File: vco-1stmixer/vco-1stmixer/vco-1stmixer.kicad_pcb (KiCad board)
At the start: 2 copper layers, 91.7 x 48.8 mm, 48 parts, among them J101 VCO Control In, J102 1st IF Out, J103 VCO Sample, J104 RF In, J105 Conn_01x02, U101 POS-200, U102 MAV-11, U103 MAV-11, U104 TUF-1H+

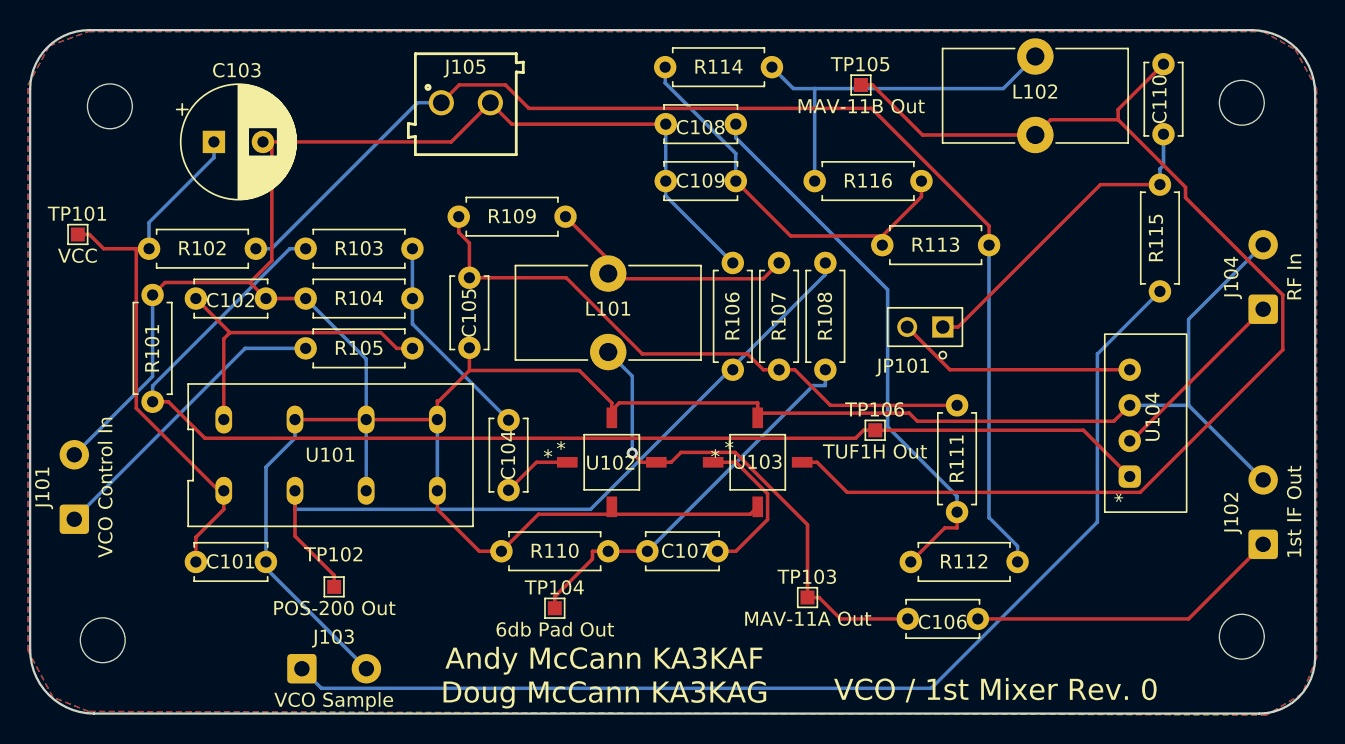
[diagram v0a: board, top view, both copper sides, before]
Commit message: minor changes to 5 boards
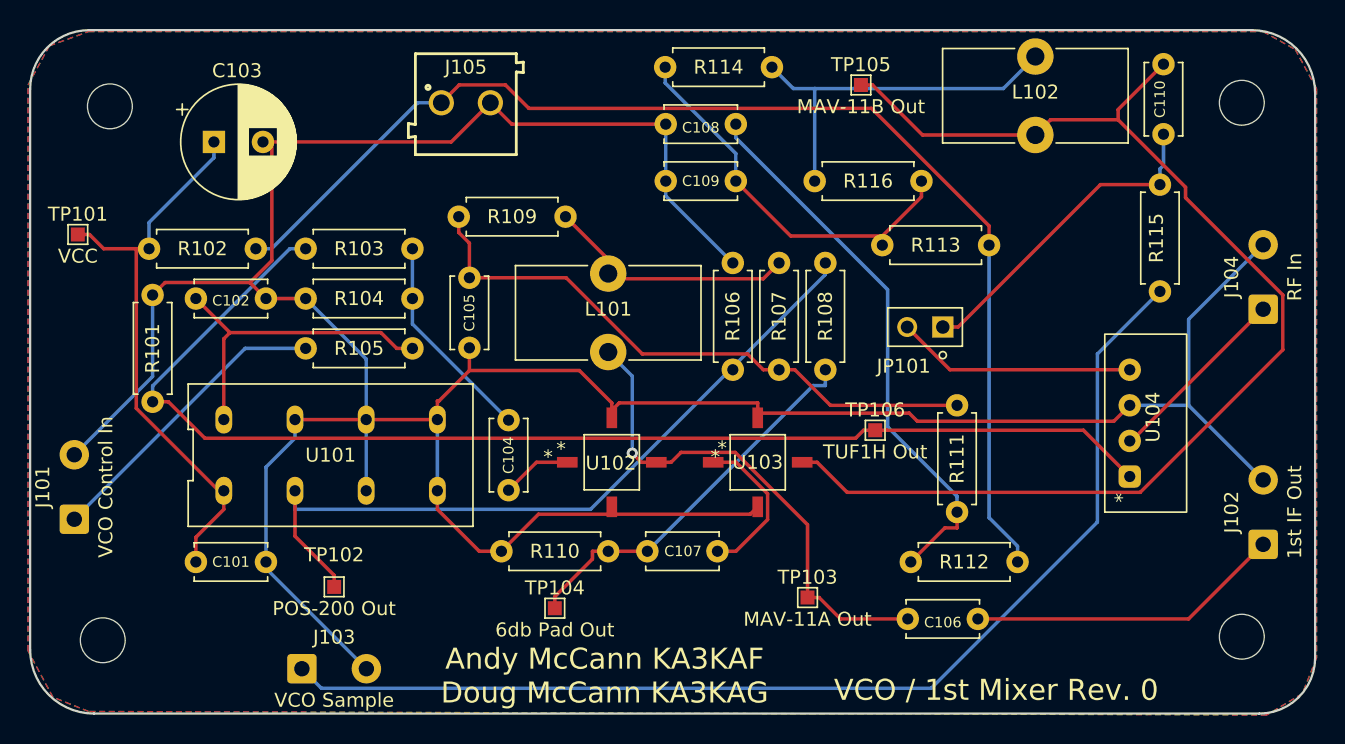
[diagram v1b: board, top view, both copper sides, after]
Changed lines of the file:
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@@
   )
   (setup
+    (stackup
+      (layer "F.SilkS" (type "Top Silk Screen"))
+      (layer "F.Paste" (type "Top Solder Paste"))
+      (layer "F.Mask" (type "Top Solder Mask") (thickness 0.01))
+      (layer "F.Cu" (type "copper") (thickness 0.035))
+      (layer "dielectric 1" (type "core") (thickness 1.51) (material "FR4") (epsilon_r 4.5) (loss_tangent 0.02))
+      (layer "B.Cu" (type "copper") (thickness 0.035))
+      (layer "B.Mask" (type "Bottom Solder Mask") (thickness 0.01))
+      (layer "B.Paste" (type "Bottom Solder Paste"))
+      (layer "B.SilkS" (type "Bottom Silk Screen"))
+      (copper_finish "None")
+      (dielectric_constraints no)
+    )
     (pad_to_mask_clearance 0)
     (grid_origin 93.687635 126.212551)
@@
     (property "Sheetfile" "vco-1stmixer.kicad_sch")
     (property "Sheetname" "")
-    (attr exclude_from_pos_files)
+    (property "exclude_from_bom" "")
+    (attr exclude_from_pos_files exclude_from_bom)
     (fp_text reference "H102" (at 0 -4.2) (layer "F.SilkS") hide
       (effects (font (size 1 1) (thickness 0.15)))
@@
     (property "Sheetfile" "vco-1stmixer.kicad_sch")
     (property "Sheetname" "")
-    (attr exclude_from_pos_files)
+    (property "exclude_from_bom" "")
+    (attr exclude_from_pos_files exclude_from_bom)
     (fp_text reference "H101" (at 0 -4.2) (layer "F.SilkS") hide
       (effects (font (size 1 1) (thickness 0.15)))
@@
     (property "Sheetfile" "vco-1stmixer.kicad_sch")
     (property "Sheetname" "")
-    (attr exclude_from_pos_files)
+    (property "exclude_from_bom" "")
+    (attr exclude_from_pos_files exclude_from_bom)
     (fp_text reference "H103" (at 0 -4.2) (layer "F.SilkS") hide
       (effects (font (size 1 1) (thickness 0.15)))
@@
     (attr through_hole)
     (fp_text reference "C110" (at 2.5 -0.254 90) (layer "F.SilkS")
-      (effects (font (size 1 1) (thickness 0.15)))
+      (effects (font (size 0.75 0.75) (thickness 0.15)))
     )
     (fp_text value ".001u" (at 2.5 2.5 90) (layer "F.Fab")
@@
     (attr through_hole)
     (fp_text reference "C109" (at 2.5 0) (layer "F.SilkS")
-      (effects (font (size 1 1) (thickness 0.15)))
+      (effects (font (size 0.75 0.75) (thickness 0.15)))
     )
     (fp_text value ".001u" (at 2.5 2.5) (layer "F.Fab")
@@
     (property "Sheetname" "")
     (attr through_hole)
-    (fp_text reference "C107" (at 2.754 0) (layer "F.SilkS")
-      (effects (font (size 1 1) (thickness 0.15)))
+    (fp_text reference "C107" (at 2.540035 0) (layer "F.SilkS")
+      (effects (font (size 0.75 0.75) (thickness 0.15)))
     )
     (fp_text value ".01u" (at 2.5 2.5) (layer "F.Fab")
@@
     (attr through_hole)
     (fp_text reference "C104" (at 2.5 0 90) (layer "F.SilkS")
-      (effects (font (size 1 1) (thickness 0.15)))
+      (effects (font (size 0.75 0.75) (thickness 0.15)))
     )
     (fp_text value ".001u" (at 2.5 2.5 90) (layer "F.Fab")
@@
     (attr through_hole)
     (fp_text reference "C101" (at 2.5 0) (layer "F.SilkS")
-      (effects (font (size 1 1) (thickness 0.15)))
+      (effects (font (size 0.75 0.75) (thickness 0.15)))
     )
     (fp_text value ".01u" (at 2.5 2.5) (layer "F.Fab")
@@
     (attr through_hole)
     (fp_text reference "C102" (at 2.5 -0.152449) (layer "F.SilkS")
-      (effects (font (size 1 1) (thickness 0.15)))
+      (effects (font (size 0.75 0.75) (thickness 0.15)))
     )
     (fp_text value ".1u" (at 2.5 2.5) (layer "F.Fab")
@@
     (attr through_hole)
     (fp_text reference "C105" (at 2.5 0 90) (layer "F.SilkS")
-      (effects (font (size 1 1) (thickness 0.15)))
+      (effects (font (size 0.75 0.75) (thickness 0.15)))
     )
     (fp_text value ".001u" (at 2.5 2.5 90) (layer "F.Fab")
@@
     (attr through_hole)
     (fp_text reference "C108" (at 2.5 0.254) (layer "F.SilkS")
-      (effects (font (size 1 1) (thickness 0.15)))
+      (effects (font (size 0.75 0.75) (thickness 0.15)))
     )
     (fp_text value ".001u" (at 2.5 2.5) (layer "F.Fab")
@@
     (property "Sheetfile" "vco-1stmixer.kicad_sch")
     (property "Sheetname" "")
-    (attr exclude_from_pos_files)
+    (property "exclude_from_bom" "")
+    (attr exclude_from_pos_files exclude_from_bom)
     (fp_text reference "H104" (at 0 -4.2) (layer "F.SilkS") hide
       (effects (font (size 1 1) (thickness 0.15)))
@@
     (attr through_hole)
     (fp_text reference "C106" (at 2.5 0.254) (layer "F.SilkS")
-      (effects (font (size 1 1) (thickness 0.15)))
+      (effects (font (size 0.75 0.75) (thickness 0.15)))
     )
     (fp_text value ".001u" (at 2.5 2.5) (layer "F.Fab")
@@
       (effects (font (size 1 1) (thickness 0.15)))
     )
-    (fp_text user "*" (at -2.032 -1.016) (layer "F.SilkS")
-      (effects (font (size 1 1) (thickness 0.15)))
-    )
+    (fp_text user "*" (at -2.539965 -1.016) (layer "F.SilkS")
+      (effects (font (size 1 1) (thickness 0.15)))
+    )

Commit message: Fix POS200 footprint and Terminal Block footprint of VCO 1st Mixer Board.  Rev 1.
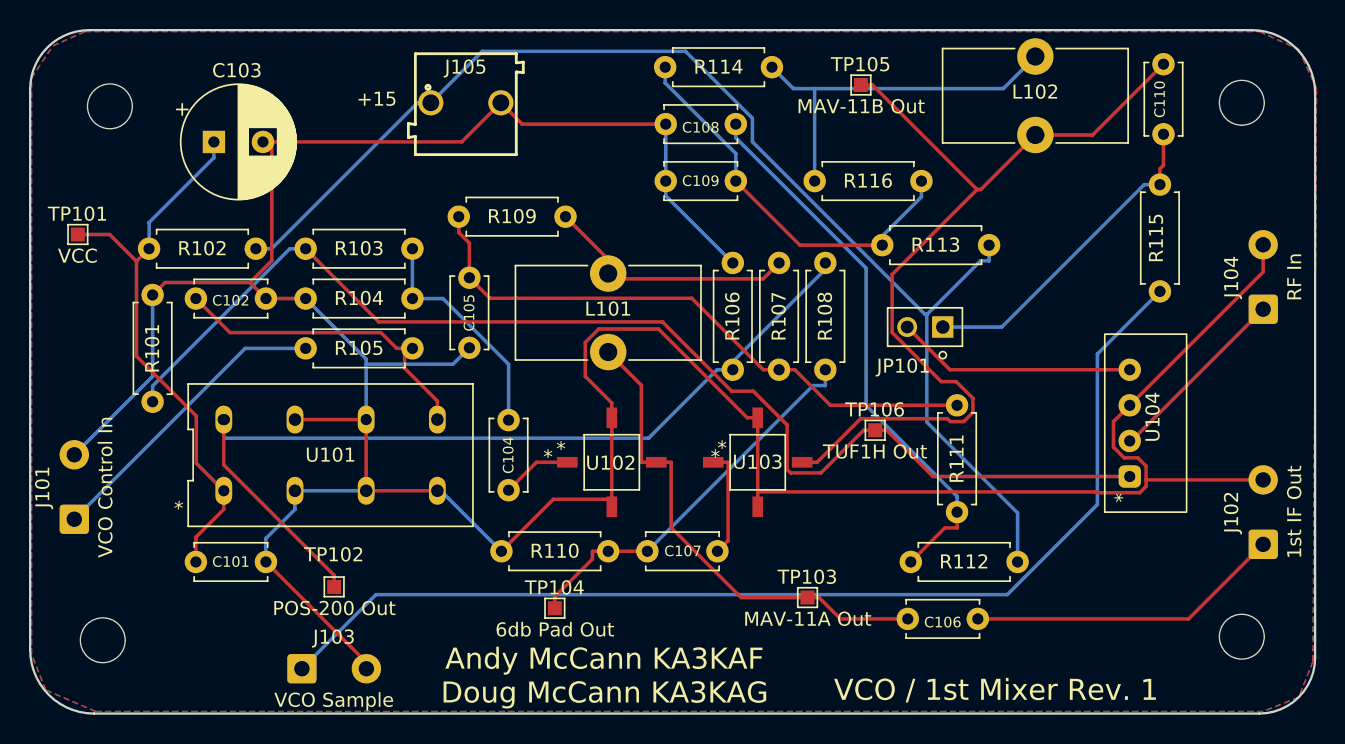
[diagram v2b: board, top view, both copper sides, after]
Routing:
- net Net-(C110-Pad2): track 86.3 -> 63.6 mm
- net Net-(R106-Pad2): track 55.1 -> 65.5 mm
- net Net-(J105-Pad1): track 86.2 -> 90.0 mm
- net Net-(C107-Pad2): track 11.2 -> 7.73 mm
- net Net-(R101-Pad2): track 88.5 -> 86.0 mm
- net GND: track 240.9 -> 243.1 mm
- net Net-(J103-Pad1): track 80.6 -> 78.7 mm
- net Net-(C104-Pad1): track 15.1 -> 16.3 mm
- net Net-(C106-Pad1): track 36.1 -> 35.2 mm, vias 1 -> 0
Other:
- board text added: "+15"
- board text added: "VCO / 1st Mixer Rev. 1"
- board text removed: "VCO / 1st Mixer Rev. 0"

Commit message: qex 1998 article and changes to vco 1st mixer pcb
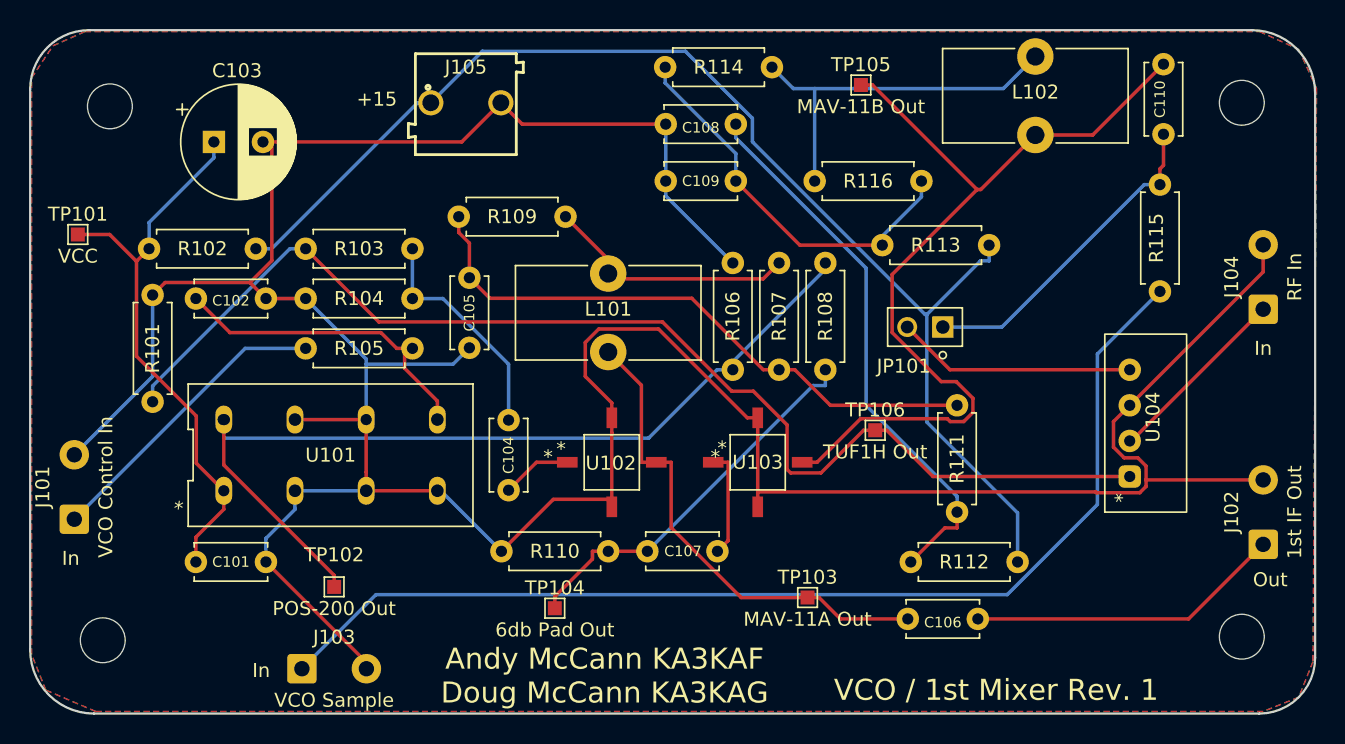
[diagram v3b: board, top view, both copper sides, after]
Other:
- board text added: "In"
- board text added: "Out"
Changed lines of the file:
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@@
+    (effects (font (size 1 1) (thickness 0.15)))
+  )
+  (gr_text "In" (at 94.957635 116.306551) (layer "F.SilkS")
+    (effects (font (size 1 1) (thickness 0.15)))
+  )
+  (gr_text "In" (at 108.546635 124.307551) (layer "F.SilkS")
     (effects (font (size 1 1) (thickness 0.15)))
   )
@@
     (effects (font (size 1.5 1.5) (thickness 0.3)))
   )
+  (gr_text "Out" (at 180.555635 117.830551) (layer "F.SilkS")
+    (effects (font (size 1 1) (thickness 0.15)))
+  )
   (gr_text "VCO / 1st Mixer Rev. 1" (at 160.997635 125.704551) (layer "F.SilkS")
     (effects (font (size 1.5 1.5) (thickness 0.3)))
   )
+  (gr_text "In" (at 180.047635 101.320551) (layer "F.SilkS")
+    (effects (font (size 1 1) (thickness 0.15)))
+  )
   (segment (start 131.675 103.3211) (end 133.5656 105.2117) (width 0.25) (layer "F.Cu") (net 1))

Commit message: Fixes to 2ndmixer-2ndlo and vco-1stmixer
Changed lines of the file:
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@@
   (gr_line (start 183.755903 123.392144) (end 183.755903 83.1226) (layer "Edge.Cuts") (width 0.16))
   (gr_arc (start 183.755903 123.392144) (mid 182.587635 126.212551) (end 179.767228 127.380819) (layer "Edge.Cuts") (width 0.16))
-  (gr_arc (start 179.246122 78.612819) (mid 182.434995 79.933716) (end 183.755903 83.1226) (layer "Edge.Cuts") (width 0.16))
+  (gr_arc (start 179.246122 78.612819) (mid 182.435001 79.933721) (end 183.755903 83.1226) (layer "Edge.Cuts") (width 0.16))
   (gr_text "+15" (at 116.801635 83.540551) (layer "F.SilkS")
     (effects (font (size 1 1) (thickness 0.15)))

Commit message: 1st mixer VCO pcb rev 2
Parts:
- added C111: .001, spectrum-analyzer:DSS1N_MUR, F.Cu at (135.7, 84.8)
- added TP107: 6db Pad Out, TestPoint:TestPoint_Pad_1.0x1.0mm, F.Cu at (153.9, 124.4)
- J103: footprint Connector_Wire:SolderWire-0.5sqmm_1x02_P4.6mm_D0.9mm_OD2.1mm -> Connector_PinHeader_2.54mm:PinHeader_1x02_P2.54mm_Vertical
- J105: value Conn_01x02 -> +15; footprint vco-1stmixer:691103110002 -> Connector_Wire:SolderWire-0.5sqmm_1x02_P4.6mm_D0.9mm_OD2.1mm
- TP103: value MAV-11A Out -> MAV-11 TUF
- TP105: value MAV-11B Out -> MAV-11 POS
- moved J103 62.1 mm to (169.6, 102.6), turned to 90 degrees
- moved R101 50.7 mm to (144.2, 123.7), turned to 90 degrees
- moved R104 44.8 mm to (148.3, 123.7), turned to 90 degrees
- moved R103 36.1 mm to (142.7, 112.8)
- moved R116 34.4 mm to (114.8, 80.7)
- moved U102 31.6 mm to (163.7, 119.1)
- moved R114 30.4 mm to (114.8, 84.3), turned to 0 degrees
- moved L101 29.7 mm to (160.7, 107.4)
- moved TP106 29.5 mm to (166.8, 81.5)
- moved R111 28.9 mm to (129.8, 110.5), turned to 0 degrees
- moved C104 28.4 mm to (151.6, 119.1), turned to 0 degrees
- moved R107 26.4 mm to (137.4, 120.4), turned to 180 degrees
- moved R113 26.1 mm to (130.8, 80.0), turned to -90 degrees
- moved R109 26.1 mm to (137.4, 117.1)
- moved C105 26.1 mm to (136.3, 123.9), turned to 180 degrees
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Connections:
- J105 pad 1: Net-(J105-Pad1) -> /+15
- R102 pad 2: Net-(J105-Pad1) -> /+15
- R112 pad 2: Net-(J105-Pad1) -> Net-(C111-Pad1)
- R113 pad 2: Net-(J105-Pad1) -> /+15
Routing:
- net GND: track 243.1 -> 0.00 mm
- net Net-(J105-Pad1): track 90.0 -> 0.00 mm
- net Net-(J103-In): track 78.7 -> 4.38 mm
- net Net-(U103-RF_Out): track 63.6 -> 24.7 mm
- net /+15: track 0.00 -> 38.9 mm
- net Net-(U104-RF): track 86.0 -> 50.4 mm
- net Net-(C108-Pad2): track 39.7 -> 7.24 mm
- net Net-(C111-Pad1): track 0.00 -> 31.7 mm
- net Net-(C105-Pad2): track 43.2 -> 15.0 mm
- net Net-(J102-In): track 22.6 -> 5.03 mm
- net Net-(C109-Pad2): track 28.3 -> 12.3 mm
- net Net-(L102-Pad1): track 27.0 -> 41.9 mm
- net Net-(U102-RF_Out): track 35.2 -> 21.4 mm
- net Net-(L101-Pad1): track 18.1 -> 30.6 mm
- net Net-(JP101-J2): track 17.1 -> 4.97 mm
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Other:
- board text added: "VCO / 1st Mixer Rev. 2"
- board text removed: "+15"
- board text removed: "VCO / 1st Mixer Rev. 1"

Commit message: minor updates
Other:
- board text added: "*"
